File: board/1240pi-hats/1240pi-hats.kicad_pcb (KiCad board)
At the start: 2 copper layers, 46.7 x 29 mm, 12 parts, among them J10 Conn_02x05_Odd_Even, J11 Conn_01x03, J20 Conn_01x03, P10 74HC74, P20 74HC04, U10 74HC74, U11 MC74VHC1G125, U12 MC74VHC1G125, U20 74HC04, U21 MC74VHC1G125

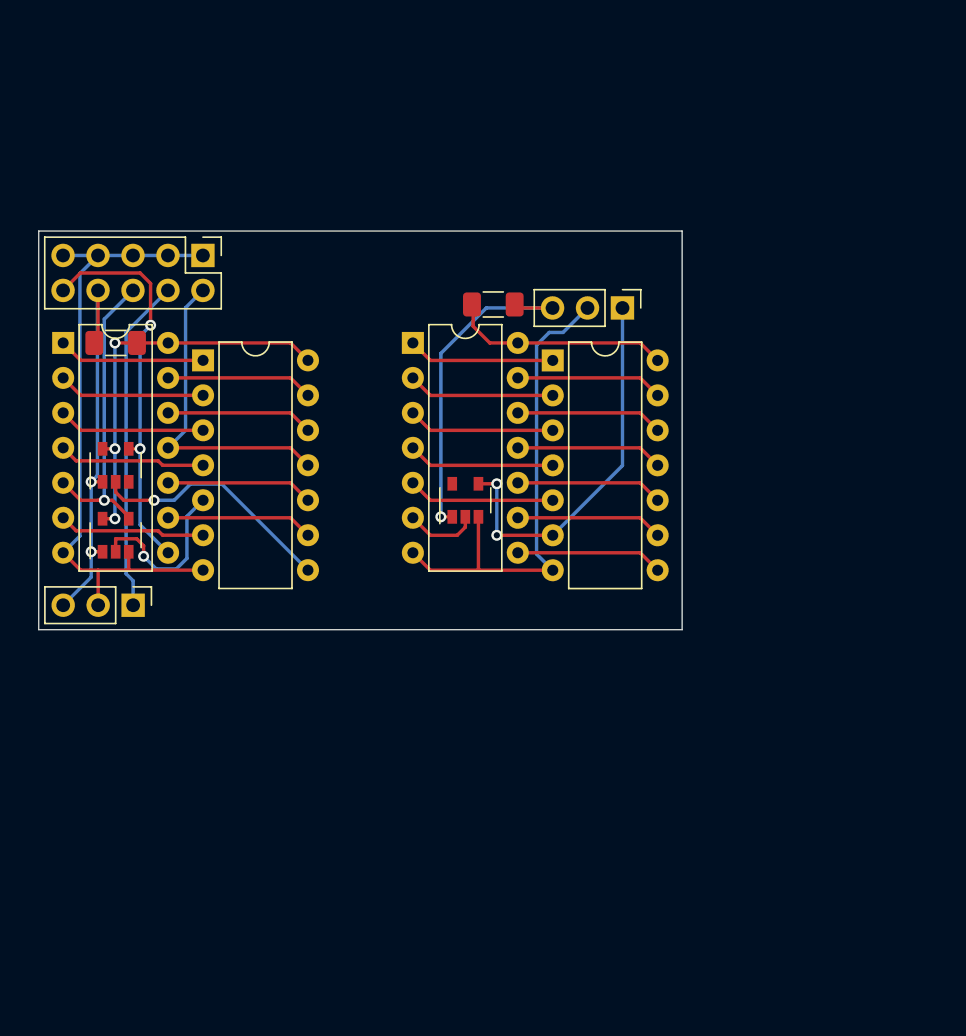
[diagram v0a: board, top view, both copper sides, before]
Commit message: Redesign display hat to use a single board.
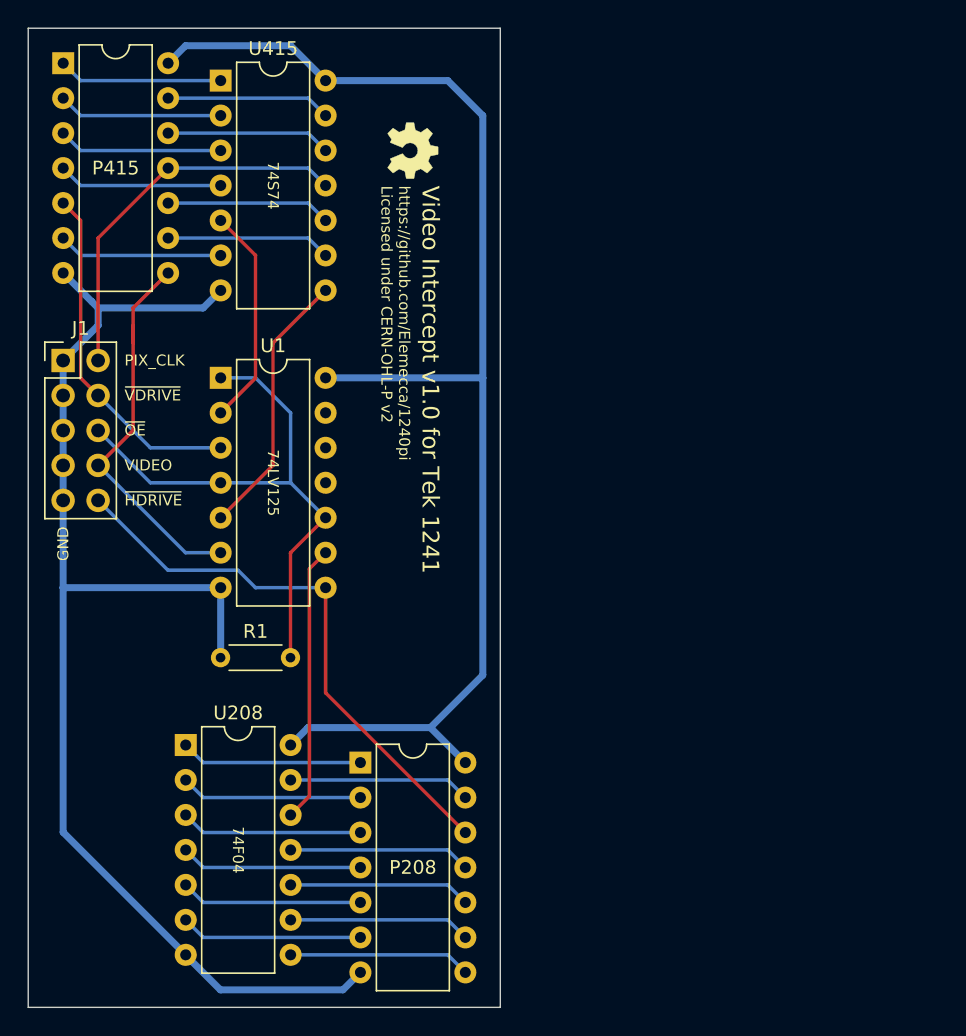
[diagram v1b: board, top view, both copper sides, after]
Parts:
- removed J10: Conn_02x05_Odd_Even, Connector_PinHeader_2.54mm:PinHeader_2x05_P2.54mm_Vertical
- removed J11, J20: Conn_01x03, Connector_PinHeader_2.54mm:PinHeader_1x03_P2.54mm_Vertical
- removed P10, U10: 74HC74, Package_DIP:DIP-14_W7.62mm
- removed P20, U20: 74HC04, Package_DIP:DIP-14_W7.62mm
- removed R10, R20: R, Resistor_SMD:R_1206_3216Metric_Pad1.30x1.75mm_HandSolder
- removed U11, U12, U21: MC74VHC1G125, 0Local:Package_SC-74A
- added J1: Conn_02x05_Odd_Even, Connector_PinHeader_2.54mm:PinHeader_2x05_P2.54mm_Vertical, F.Cu at (101.6, 72.4)
- added OSHW: LOGO, 0Local:OSHW, F.Cu at (127.0, 57.1)
- added P208: Header, Package_DIP:DIP-14_W7.62mm, F.Cu at (123.2, 101.6)
- added P415: Header, Package_DIP:DIP-14_W7.62mm, F.Cu at (101.6, 50.8)
- added R1: R, Resistor_THT:R_Axial_DIN0204_L3.6mm_D1.6mm_P5.08mm_Horizontal, F.Cu at (118.1, 94.0)
- added U1: 74LV125, Package_DIP:DIP-14_W7.62mm, F.Cu at (113.0, 73.7)
- added U208: 74F04, Package_DIP:DIP-14_W7.62mm, F.Cu at (110.5, 100.3)
- added U415: 74S74, Package_DIP:DIP-14_W7.62mm, F.Cu at (113.0, 52.1)
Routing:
- net +5V: track 45.1 -> 97.2 mm, vias 3 -> 0
- net /Display/~{OE}: track 0.00 -> 41.6 mm
- net /Display/~{HDRIVE}: track 0.00 -> 41.1 mm
- net /Display U208/~{HDRIVE}: track 33.1 -> 0.00 mm, vias 2 -> 0
- net /Display U415/~{OE}: track 29.9 -> 0.00 mm, vias 2 -> 0
- net /Display/VIDEO: track 0.00 -> 28.9 mm
- net /Display U415/VIDEO: track 28.8 -> 0.00 mm, vias 2 -> 0
- net /Display/PIX_CLK: track 0.00 -> 28.0 mm
- net /Display/~{VDRIVE}: track 0.00 -> 25.4 mm
- net /Display U208/~{OE}: track 25.2 -> 0.00 mm, vias 1 -> 0
- net /Display U415/~{HDRIVE}: track 24.3 -> 0.00 mm
- net /Display U415/PIX_CLK: track 23.2 -> 0.00 mm
- net /Display U415/~{VDRIVE}: track 22.0 -> 0.00 mm, vias 1 -> 0
- net Net-(U1-Pad9): track 0.00 -> 20.1 mm
- net Net-(U415-Pad8): track 0.00 -> 19.7 mm
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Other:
- board size 46.7 x 29 mm -> 34.3 x 71.1 mm
- board text added: "GND"
- board text added: "PIX_CLK"
- board text added: "VIDEO"
- board text added: "Video Intercept v1.0 for Tek 1241"
- board text added: "https://github.com/Elemecca/1240pi Licensed under CERN-OHL-P v2"
- board text added: "~{HDRIVE}"
- board text added: "~{OE}"
- board text added: "~{VDRIVE}"

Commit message: Finish up display hat board.
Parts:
- R1: value R -> 4k7; footprint Resistor_THT:R_Axial_DIN0204_L3.6mm_D1.6mm_P5.08mm_Horizontal -> Resistor_THT:R_Axial_DIN0207_L6.3mm_D2.5mm_P10.16mm_Horizontal
- U1: value 74LV125 -> 74F126
- moved R1 10.2 mm to (128.3, 94.6)
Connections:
- J1 pad 10: /Display/~{HDRIVE} -> /Display/~{VDRIVE}
- J1 pad 2: /Display/PIX_CLK -> /Display/~{EXT_EN}
- J1 pad 4: /Display/~{VDRIVE} -> /Display/PIX_CLK
- J1 pad 6: /Display/~{OE} -> /Display/VIDEO
- J1 pad 8: /Display/VIDEO -> /Display/~{HDRIVE}
- R1 pad 1: /Display/~{OE} -> +5V
- R1 pad 2: GND -> /Display/~{EXT_EN}
- U1 pad 1: /Display/~{OE} -> /Display/~{EXT_EN}
- U1 pad 10: /Display/~{OE} -> /Display/~{EXT_EN}
- U1 pad 11: (no net) -> unconnected-(U1-Pad11)
- U1 pad 12: (no net) -> GND
- U1 pad 13: (no net) -> GND
- U1 pad 2: Net-(U415-Pad5) -> Net-(U415-Pad8)
- U1 pad 3: /Display/~{VDRIVE} -> /Display/VIDEO
- U1 pad 4: /Display/~{OE} -> /Display/~{EXT_EN}
- U1 pad 5: Net-(U415-Pad8) -> Net-(U415-Pad5)
- U1 pad 6: /Display/VIDEO -> /Display/~{VDRIVE}
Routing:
- net /Display/~{OE}: track 41.6 -> 0.00 mm
- net /Display/~{EXT_EN}: track 0.00 -> 41.2 mm
- net +5V: track 97.2 -> 85.0 mm
- net GND: track 95.6 -> 106.3 mm
- net /Display/~{VDRIVE}: track 25.4 -> 33.1 mm
- net Net-(U415-Pad8): track 19.7 -> 12.1 mm
- net Net-(U415-Pad5): track 16.1 -> 23.2 mm
- net /Display/VIDEO: track 28.9 -> 23.0 mm
- net /Display/PIX_CLK: track 28.0 -> 30.6 mm
- net /Display/~{HDRIVE}: track 41.1 -> 42.2 mm
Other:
- board text added: "~{EXT_EN}"
- board text removed: "~{OE}"

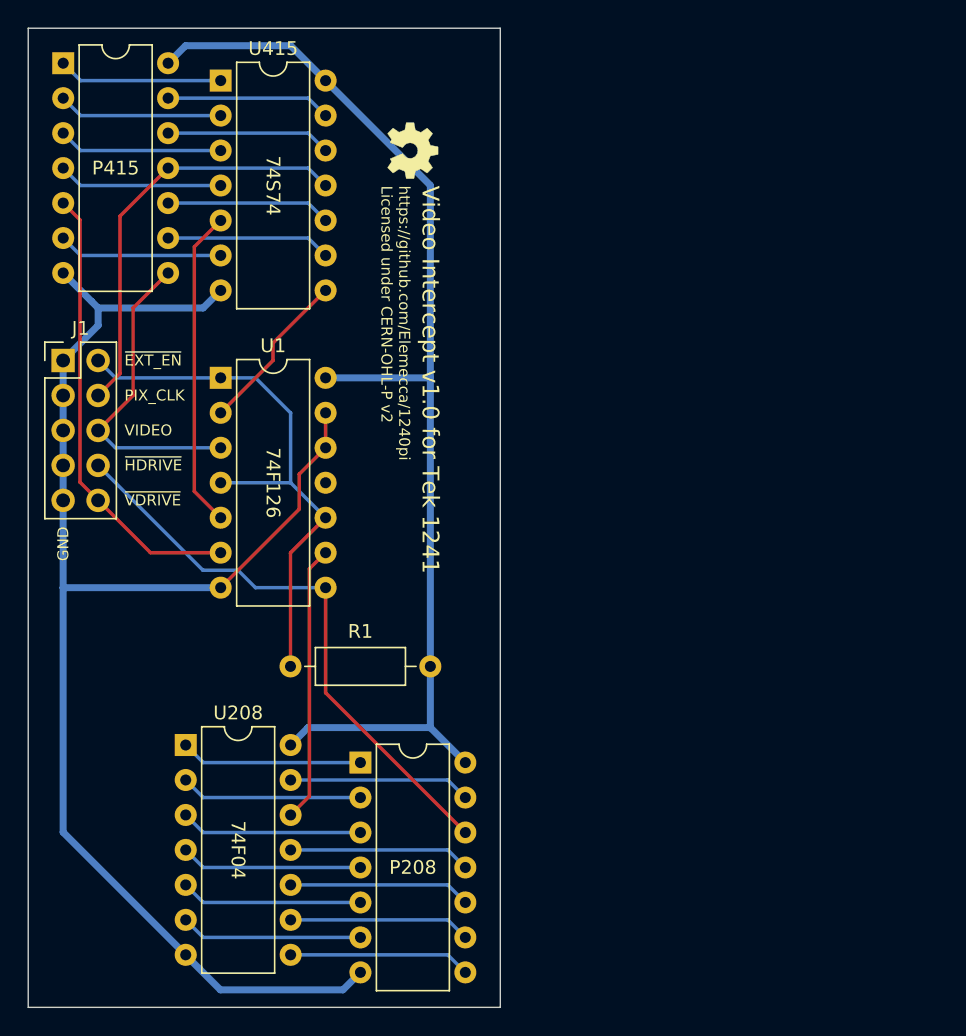
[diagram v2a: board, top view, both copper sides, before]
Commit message: Add IO Processor hat board.
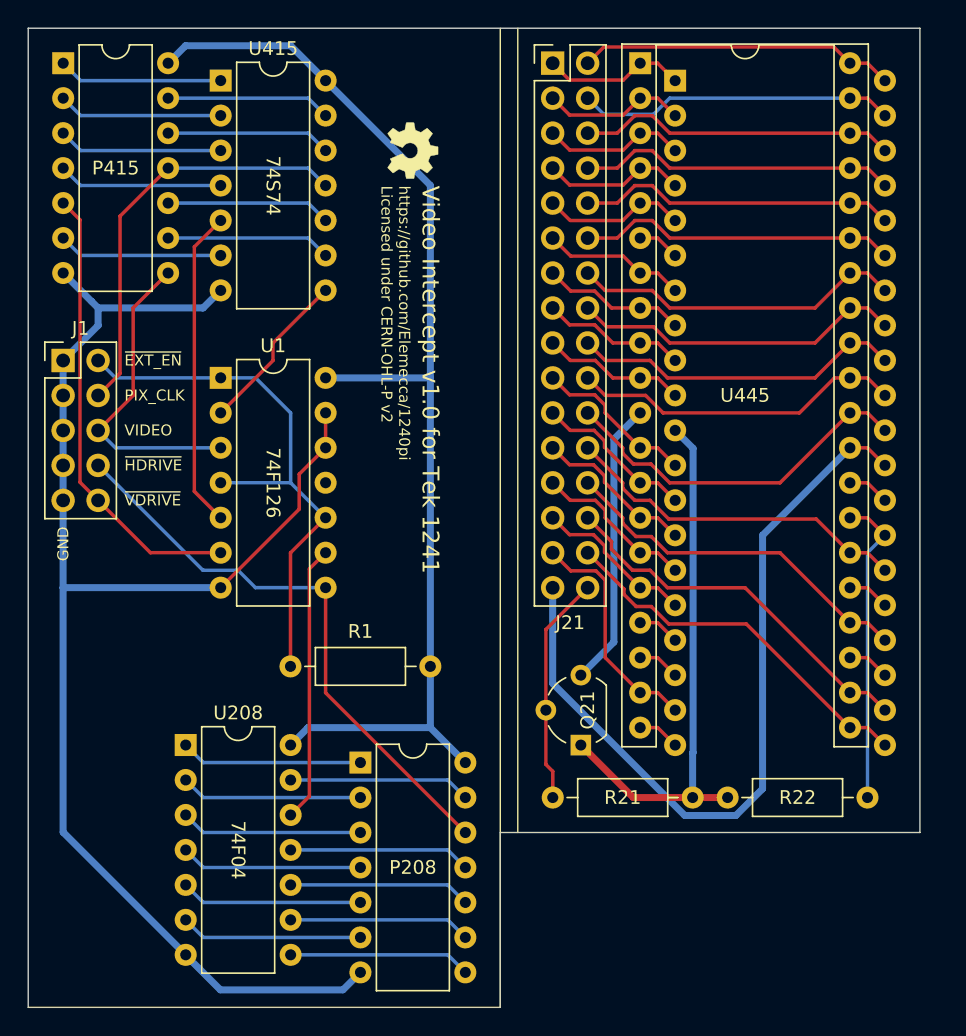
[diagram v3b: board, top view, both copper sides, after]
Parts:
- added J21: Conn_02x16_Odd_Even, Connector_PinHeader_2.54mm:PinHeader_2x16_P2.54mm_Vertical, F.Cu at (137.2, 50.8)
- added P445: Header, Package_DIP:DIP-40_W15.24mm, F.Cu at (146.0, 52.1)
- added Q21: Q_PMOS_SGD, Package_TO_SOT_THT:TO-92_Wide, F.Cu at (139.2, 100.3)
- added R21: 10k, Resistor_THT:R_Axial_DIN0207_L6.3mm_D2.5mm_P10.16mm_Horizontal, F.Cu at (147.3, 104.1)
- added R22: 10k, Resistor_THT:R_Axial_DIN0207_L6.3mm_D2.5mm_P10.16mm_Horizontal, F.Cu at (149.9, 104.1)
- added U445: Z80, Package_DIP:DIP-40_W15.24mm_Socket, F.Cu at (143.5, 50.8)
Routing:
- net GND: track 106.3 -> 163.8 mm
- net +5V: track 85.0 -> 124.5 mm
- net /IO Processor/~{WR}: track 0.00 -> 27.7 mm
- net /IO Processor/~{RD}: track 0.00 -> 27.6 mm
- net /IO Processor/~{WAIT}: track 0.00 -> 26.6 mm
- net /IO Processor/A0: track 0.00 -> 26.6 mm
- net /IO Processor/~{RESET}: track 0.00 -> 25.5 mm
- net /IO Processor/A1: track 0.00 -> 24.2 mm
- net /IO Processor/A3: track 0.00 -> 24.2 mm
- net /IO Processor/A2: track 0.00 -> 24.2 mm
- net /IO Processor/A4: track 0.00 -> 24.2 mm
- net /IO Processor/A8: track 0.00 -> 23.2 mm
- net /IO Processor/A7: track 0.00 -> 23.2 mm
- net /IO Processor/A6: track 0.00 -> 23.2 mm
- net /IO Processor/A5: track 0.00 -> 23.2 mm
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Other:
- board size 34.3 x 71.1 mm -> 64.8 x 71.1 mm

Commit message: Add tabs to hats board.
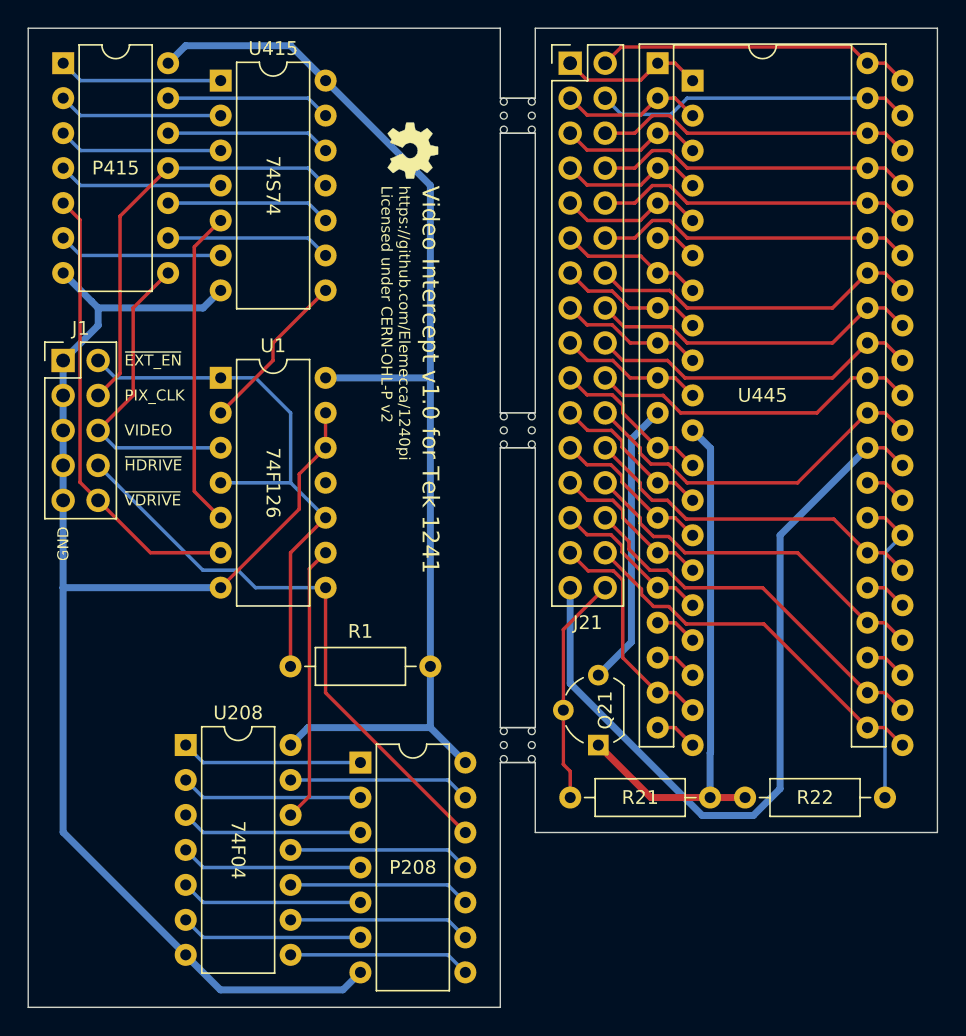
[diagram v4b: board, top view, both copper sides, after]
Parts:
- added REF**: Panel_Tab, 0Local:Panel_Tab, F.Cu at (133.3, 53.3)
- added REF**: Panel_Tab, 0Local:Panel_Tab, F.Cu at (133.3, 76.2)
- added REF**: Panel_Tab, 0Local:Panel_Tab, F.Cu at (133.3, 99.1)
- moved J21 1.27 mm to (138.4, 50.8)
- moved P445 1.27 mm to (147.3, 52.1)
- moved Q21 1.27 mm to (140.5, 100.3)
- moved R21 1.27 mm to (148.6, 104.1)
- moved U445 1.27 mm to (144.8, 50.8)
- moved R22 1.27 mm to (151.1, 104.1)
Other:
- board size 64.8 x 71.1 mm -> 66 x 71.1 mm
